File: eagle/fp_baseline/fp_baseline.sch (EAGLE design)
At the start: 2 parts

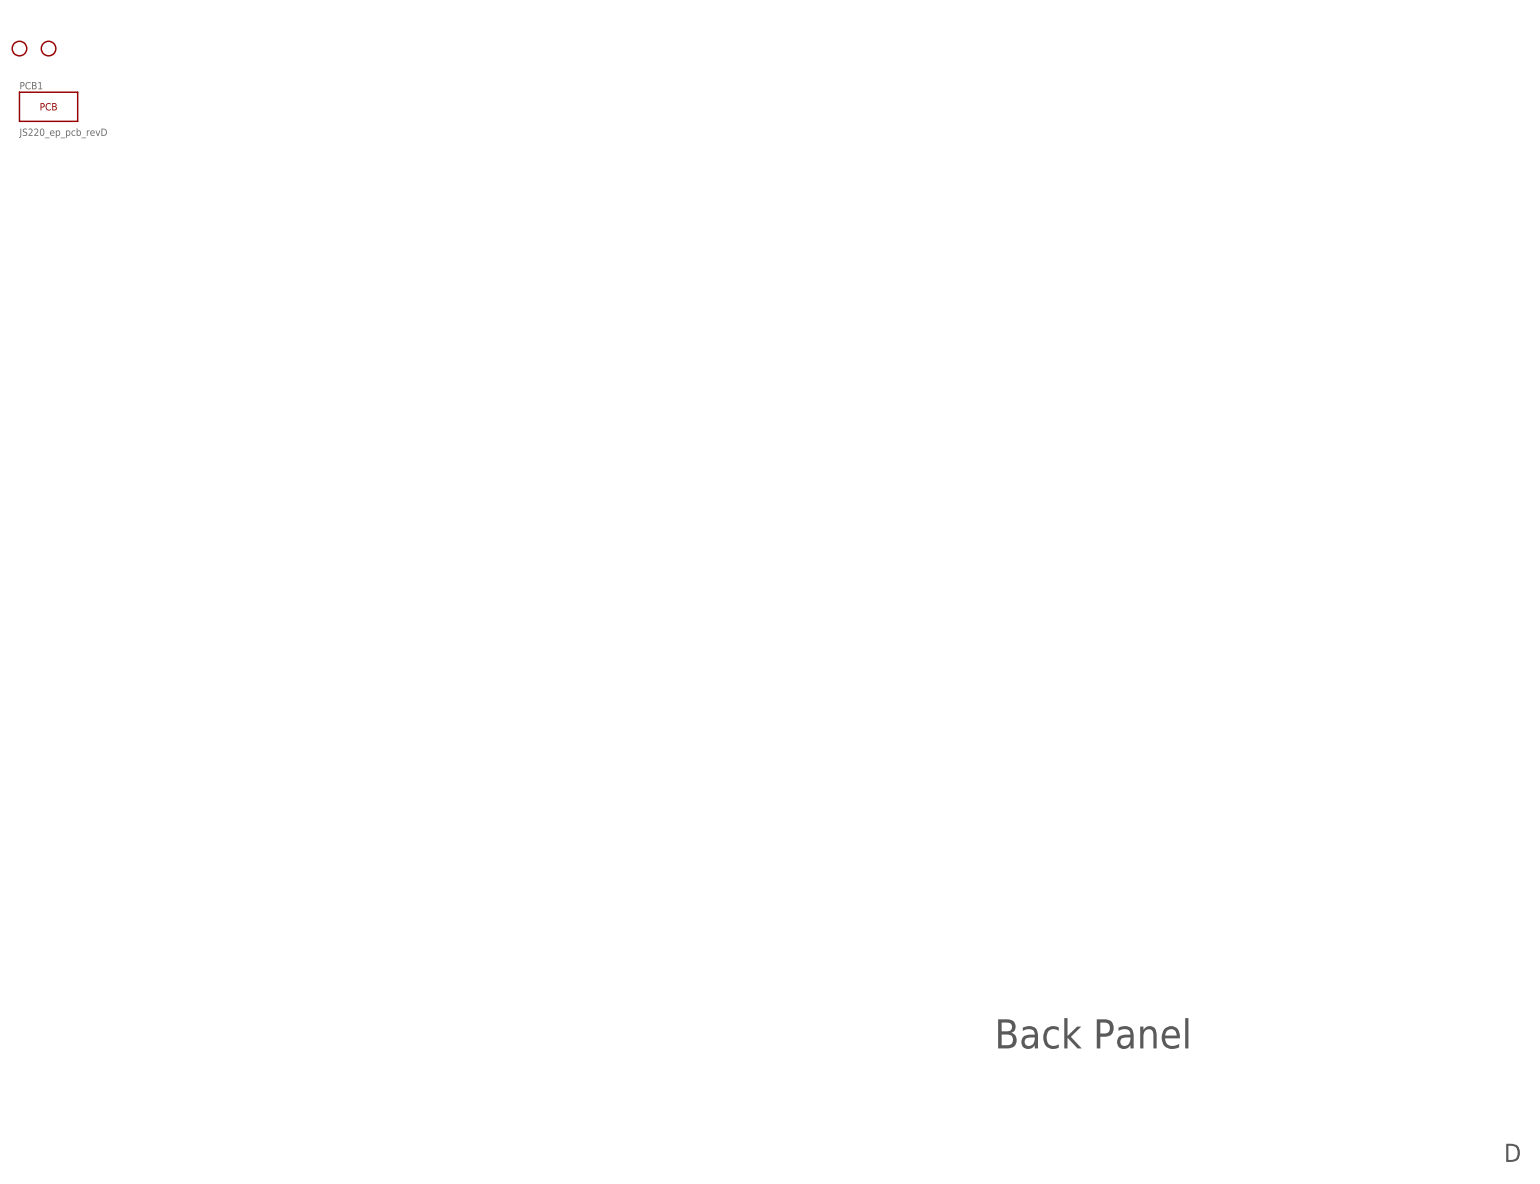
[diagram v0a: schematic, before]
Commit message: Updates for JS220 first production build.
* Updated back panel for production build.
  * Increased USB hole size by 0.2 mm in left, right, and up directions
  * Bumped rev from C to D.
* Added additional boards:
  * fb_usb2_ba: USB 2.0 B/A connector
  * fp_bnc: BNC & 0.1" headers
  * fp_js110: Safety banana jacks configured like the JS110.
  * fp_baseline: Starting point for creating new boards in Eagle.
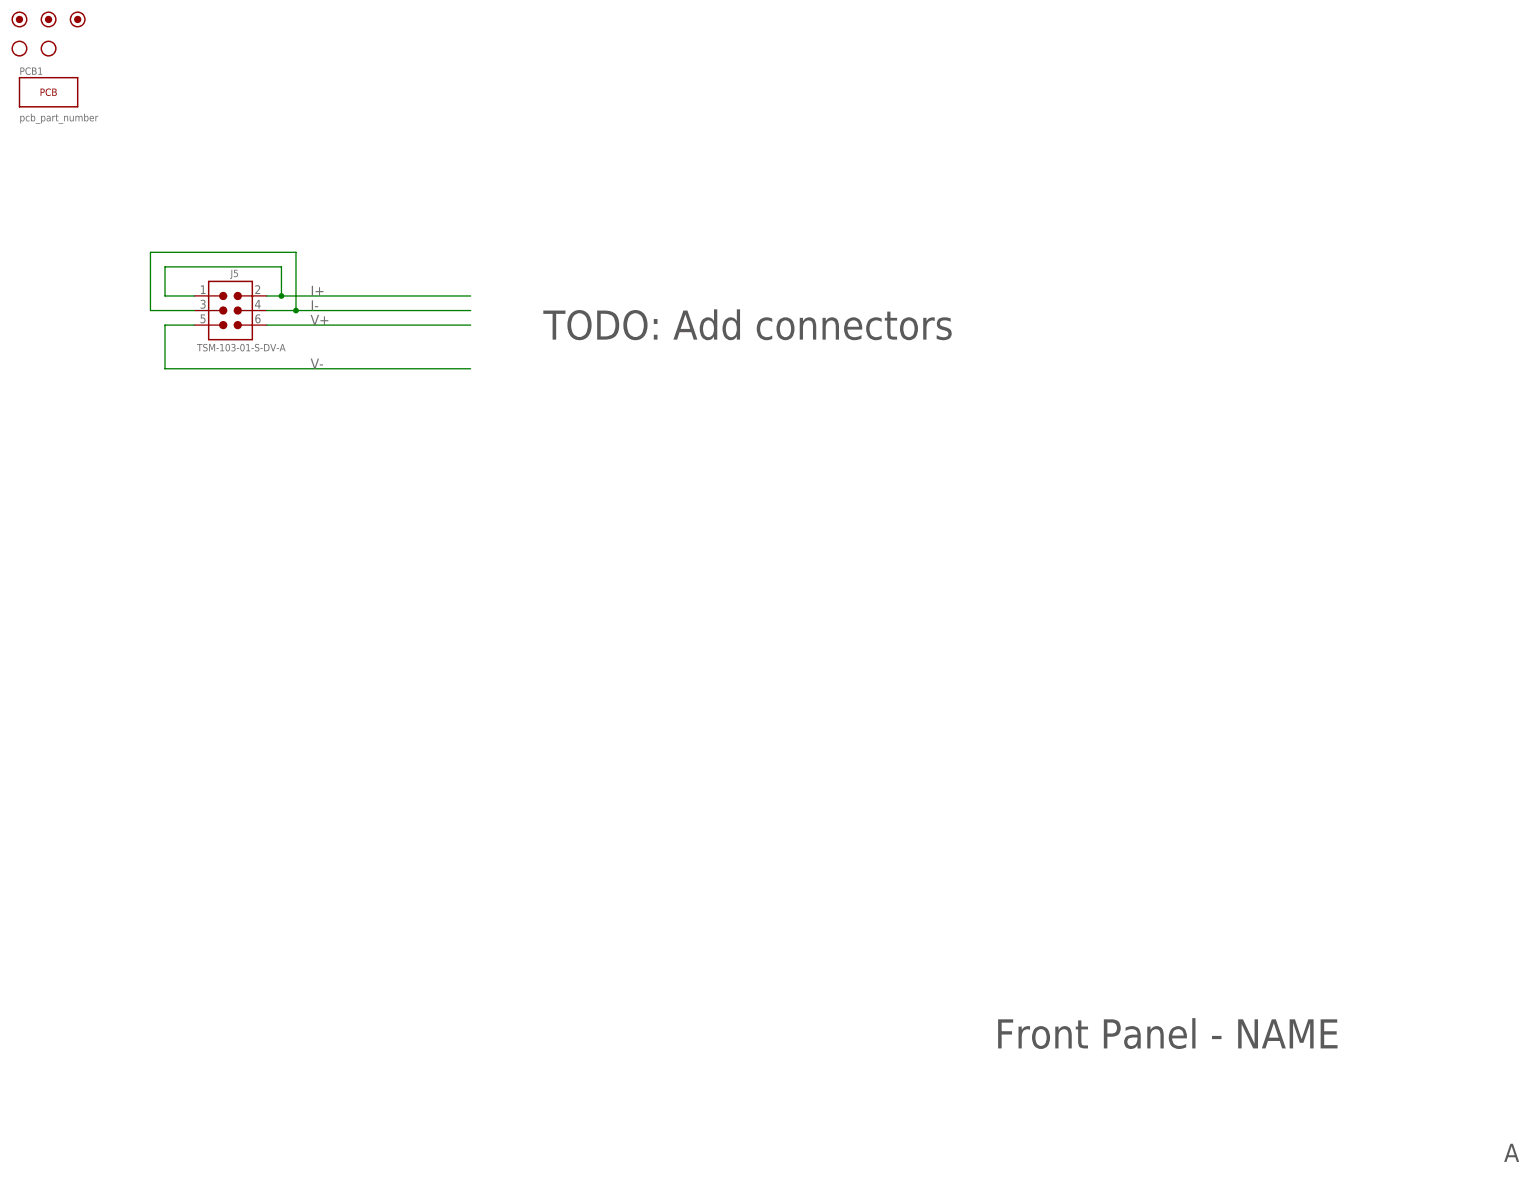
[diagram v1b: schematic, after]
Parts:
- added FUD1, FUD2, FUD3: FIDUCIAL_1MM, jetperch:FIDUCIAL_1MM
- added J5: TSM-103-01-S-DV-A, jetperch:CONN_0.1_3X2_MSA
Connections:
- new net I+: J5.1, J5.2
- new net I-: J5.3, J5.4
- new net V+: J5.6
- new net V-: J5.5
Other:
- note added: "A"
- note added: "Front Panel - NAME"
- note added: "TODO: Add connectors"
- note removed: "Back Panel"
- note removed: "D"
- moved on the sheet: PCB1
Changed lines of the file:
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@@
 <parts>
 <part name="FRAME1" library="frames" library_urn="urn:adsk.eagle:library:229" deviceset="FRAME_A_L" device="" value="PG1"/>
+<part name="J5" library="jetperch" deviceset="CONN_0.1_3X2" device="_MSA" value="TSM-103-01-S-DV-A">
+<attribute name="MPN" value="TSM-103-01-S-DV-A"/>
+<attribute name="POPULATE" value="1"/>
+</part>
+<part name="FUD1" library="jetperch" deviceset="FIDUCIAL" device="_1MM"/>
+<part name="FUD2" library="jetperch" deviceset="FIDUCIAL" device="_1MM"/>
+<part name="FUD3" library="jetperch" deviceset="FIDUCIAL" device="_1MM"/>
 <part name="H1" library="jetperch" deviceset="HOLE" device="_#6_NORESTRICT" value="HOLE_#6_NORESTRICT">
 <attribute name="POPULATE" value="0"/>
@@
 <attribute name="POPULATE" value="0"/>
 </part>
-<part name="PCB1" library="jetperch" deviceset="PCB" device="" value="JS220_ep_pcb_revD">
+<part name="PCB1" library="jetperch" deviceset="PCB" device="" value="pcb_part_number">
 <attribute name="POPULATE" value="1"/>
 </part>
@@
 <sheet>
 <plain>
-<text x="177.8" y="26.162" size="5.08" layer="97">Back Panel</text>
-<text x="266.7" y="6.35" size="3.175" layer="97">D</text>
+<text x="177.8" y="26.162" size="5.08" layer="97">Front Panel - NAME</text>
+<text x="266.7" y="6.35" size="3.175" layer="97">A</text>
+<text x="99.06" y="149.86" size="5.08" layer="97">TODO: Add connectors</text>
 </plain>
 <instances>
@@
 <attribute name="DRAWING_NAME" x="190.5" y="19.05" size="2.54" layer="94"/>
 </instance>
+<instance part="J5" gate="G1" x="45.72" y="154.94" smashed="yes">
+<attribute name="MPN" x="45.72" y="154.94" size="1.778" layer="96" display="off"/>
+<attribute name="POPULATE" x="45.72" y="154.94" size="1.778" layer="96" display="off"/>
+<attribute name="NAME" x="44.45" y="160.782" size="1.27" layer="95"/>
+<attribute name="VALUE" x="38.608" y="147.828" size="1.27" layer="96"/>
+</instance>
+<instance part="FUD1" gate="G$1" x="7.62" y="205.74" smashed="yes"/>
+<instance part="FUD2" gate="G$1" x="12.7" y="205.74" smashed="yes"/>
+<instance part="FUD3" gate="G$1" x="17.78" y="205.74" smashed="yes"/>
 <instance part="H1" gate="G$1" x="7.62" y="200.66" smashed="yes">
 <attribute name="POPULATE" x="7.62" y="200.66" size="1.778" layer="96" display="off"/>
@@
 <attribute name="POPULATE" x="12.7" y="200.66" size="1.778" layer="96" display="off"/>
 </instance>
-<instance part="PCB1" gate="G$1" x="12.7" y="190.5" smashed="yes">
-<attribute name="VALUE" x="7.62" y="185.42" size="1.27" layer="96"/>
-<attribute name="NAME" x="7.62" y="193.548" size="1.27" layer="95"/>
-<attribute name="POPULATE" x="12.7" y="190.5" size="1.27" layer="96" display="off"/>
+<instance part="PCB1" gate="G$1" x="12.7" y="193.04" smashed="yes">
+<attribute name="VALUE" x="7.62" y="187.96" size="1.27" layer="96"/>
+<attribute name="NAME" x="7.62" y="196.088" size="1.27" layer="95"/>
+<attribute name="POPULATE" x="12.7" y="193.04" size="1.27" layer="96" display="off"/>
 </instance>
 </instances>
@@
 </busses>
 <nets>
+<net name="I+" class="0">
+<segment>
+<label x="58.42" y="157.48" size="1.778" layer="95"/>
+<wire x1="53.34" y1="157.48" x2="86.36" y2="157.48" width="0.1524" layer="91"/>
+<pinref part="J5" gate="G1" pin="1"/>
+<wire x1="38.1" y1="157.48" x2="33.02" y2="157.48" width="0.1524" layer="91"/>
+<wire x1="33.02" y1="157.48" x2="33.02" y2="162.56" width="0.1524" layer="91"/>
+<wire x1="33.02" y1="162.56" x2="53.34" y2="162.56" width="0.1524" layer="91"/>
+<wire x1="53.34" y1="162.56" x2="53.34" y2="157.48" width="0.1524" layer="91"/>
+<junction x="53.34" y="157.48"/>
+<pinref part="J5" gate="G1" pin="2"/>
+<wire x1="53.34" y1="157.48" x2="50.8" y2="157.48" width="0.1524" layer="91"/>
+</segment>
+</net>
+<net name="V-" class="0">
+<segment>
+<pinref part="J5" gate="G1" pin="5"/>
+<wire x1="38.1" y1="152.4" x2="33.02" y2="152.4" width="0.1524" layer="91"/>
+<wire x1="33.02" y1="152.4" x2="33.02" y2="144.78" width="0.1524" layer="91"/>
+<wire x1="33.02" y1="144.78" x2="86.36" y2="144.78" width="0.1524" layer="91"/>
+<label x="58.42" y="144.78" size="1.778" layer="95"/>
+</segment>
+</net>
+<net name="I-" class="0">
+<segment>
+<label x="58.42" y="154.94" size="1.778" layer="95"/>
+<wire x1="50.8" y1="154.94" x2="55.88" y2="154.94" width="0.1524" layer="91"/>
+<wire x1="55.88" y1="154.94" x2="86.36" y2="154.94" width="0.1524" layer="91"/>
+<pinref part="J5" gate="G1" pin="4"/>
+<pinref part="J5" gate="G1" pin="3"/>
+<wire x1="38.1" y1="154.94" x2="30.48" y2="154.94" width="0.1524" layer="91"/>
+<wire x1="30.48" y1="154.94" x2="30.48" y2="165.1" width="0.1524" layer="91"/>
+<wire x1="30.48" y1="165.1" x2="55.88" y2="165.1" width="0.1524" layer="91"/>
+<wire x1="55.88" y1="165.1" x2="55.88" y2="154.94" width="0.1524" layer="91"/>
+<junction x="55.88" y="154.94"/>
+</segment>
+</net>
+<net name="V+" class="0">
+<segment>
+<pinref part="J5" gate="G1" pin="6"/>
+<wire x1="50.8" y1="152.4" x2="86.36" y2="152.4" width="0.1524" layer="91"/>
+<label x="58.42" y="152.4" size="1.778" layer="95"/>
+</segment>
+</net>
 </nets>
 </sheet>
